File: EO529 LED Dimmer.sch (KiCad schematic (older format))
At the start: 47 parts, among them J1 VBat, Q1 BC639, Q2 BC639, Q3 BC639, Q4 BC639, U1 NE556, U2 NE556

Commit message: Revision to circuit
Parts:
- removed C2: 10n, Capacitor_THT:C_Disc_D5.0mm_W2.5mm_P5.00mm, symbol Device:C_Small
- removed D1, D2, D3, D4, D6, D7, D8, D9: 1N4148, Diode_THT:D_DO-35_SOD27_P7.62mm_Horizontal, symbol Device:D_Small
- removed D10: LED_RGBA, LED_THT:LED_BL-FL7680RGB, symbol Device:LED_RGBA
- removed D5: White, LED_THT:LED_D10.0mm, symbol Device:LED_Small
- removed R6: 1k, Resistor_THT:R_Axial_DIN0207_L6.3mm_D2.5mm_P7.62mm_Horizontal, symbol Device:R_Small
- added C3: 10n, Capacitor_THT:C_Disc_D5.0mm_W2.5mm_P5.00mm, symbol Device:C_Small
- added D1: White, LED_THT:LED_D10.0mm, symbol Device:LED_Small
- added D2: LED_RGBA, LED_THT:LED_BL-FL7680RGB, symbol Device:LED_RGBA
- added R13, R14, R19, R20: 10k, Resistor_THT:R_Axial_DIN0207_L6.3mm_D2.5mm_P7.62mm_Horizontal, symbol Device:R_Small
- added R15, R16, R21, R22, R3: 100k, Resistor_THT:R_Axial_DIN0207_L6.3mm_D2.5mm_P7.62mm_Horizontal, symbol Device:R_Small
- added R17, R23: 1k, Resistor_THT:R_Axial_DIN0207_L6.3mm_D2.5mm_P7.62mm_Horizontal, symbol Device:R_Small
- added R18: 180, Resistor_THT:R_Axial_DIN0207_L6.3mm_D2.5mm_P7.62mm_Horizontal, symbol Device:R_Small
- added R24: 220, Resistor_THT:R_Axial_DIN0207_L6.3mm_D2.5mm_P7.62mm_Horizontal, symbol Device:R_Small
- added U3: LM339, Package_DIP:DIP-14_W7.62mm_Socket, symbol Comparator:LM339
- R1: renamed from R3; value 1k -> 10k
- R10: value 180 -> 100k
- R11: value 220 -> 1k
- R2, R7, R8: value 1k -> 10k
- R4, R9: value 1k -> 100k
- renumbered C3 to C2, R1 to R5, R5 to R6
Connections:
- net Blue: now also D2.3 (BK), R24.2; no longer R12.2
- net GND: now also R10.2, R4.2, C3.2, R16.2, R22.2, U3.12 (V-)
- net Green: now also R12.2, D2.2 (GK); no longer R11.2
- net Red: now also D2.1 (RK)
- net VCC: now also R7.1, D1.2 (A), D2.4 (A), R13.1, R15.1, R19.1, R21.1, R3.1, U3.3 (V+); no longer R4.1, R8.1
- net at R1.2, U1.1 (DIS): now also R2.1
- net at C2.1, U1.2 (THR), U1.6 (TR): now also R2.2, U3.4 (-); no longer RV1.2
- net at U1.5 (Q): no longer R5.2
- net at R8.2: now also C4.1, U1.12 (THR), U1.8 (TR), U3.6 (-); no longer U2.1 (DIS)
- net at U2.2 (THR), U2.6 (TR): now also C6.1, R14.2, U3.8 (-); no longer C7.1, RV3.2
- net at RV1.1: now also R4.1
- net at RV1.3: now also R3.2
- net at RV3.1: now also R16.1
- net at Q3.3 (B): now also R17.1
- net at R11.1: now also Q2.3 (B); no longer Q4.2 (C)
- net at RV3.3: now also R15.2
- net at R12.1: now also Q2.2 (C); no longer Q3.2 (C)
- net at U1.11 (CV): now also C3.1
- net at U1.13 (DIS): now also R7.2, R8.1; no longer R4.2
- net at U1.9 (Q): no longer R2.2
- net at U2.11 (CV): now also C7.1; no longer C6.1
- net at C8.1, U2.12 (THR), U2.8 (TR): now also R20.2, U3.10 (-); no longer RV4.2
- net at R9.2: now also RV2.3; no longer U2.13 (DIS)
- net at U2.9 (Q): no longer R7.2
- net at RV2.1: now also R10.1
- net at RV4.1: now also R22.1
- net at Q4.3 (B): now also R23.1; no longer R7.1
- net at RV4.3: now also R21.2
- new net: RV1.2, U3.5 (+)
- new net: R5.2, U3.2
- new net: R11.2, U3.1
- new net: RV2.2, U3.7 (+)
- new net: R13.2, R14.1, U2.1 (DIS)
- new net: R17.2, U3.14
- new net: RV3.2, U3.9 (+)
- new net: Q3.2 (C), R18.1
- new net: D1.1 (K), R18.2
- new net: R19.2, R20.1, U2.13 (DIS)
- new net: R23.2, U3.13
- new net: RV4.2, U3.11 (+)
- new net: Q4.2 (C), R24.1
- no-connect marks 0 -> 4
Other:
- moved on the sheet: C1, C10, C2, C9, H1, H2, H3, H4, J1, Q1, R1, R5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

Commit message: Fixed broken files
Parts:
- removed U3: LM339, Package_DIP:DIP-14_W7.62mm_Socket, symbol Comparator:LM339
- added U3, U4: LM393, Package_DIP:DIP-8_W7.62mm_Socket, symbol Comparator:LM393
- R24: value 220 -> 150
- R6: value 150 -> 220
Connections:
- net Blue: now also R12.2; no longer R24.2
- net GND: now also U3.4 (V-), U4.4 (V-)
- net Green: now also R6.2; no longer R12.2
- net Red: now also R24.2; no longer R6.2
- net VCC: now also U3.8 (V+), U4.8 (V+)
- net at C2.1, R2.2, U1.2 (THR)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: now also U3.6 (_)
- net at RV1.2: now also U3.5 (+)
- net at R5.2: now also U3.7
- net at C4.1, R8.2, U1.12 (THR)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: now also U4.2 (-)
- net at R11.2: now also U4.1
- net at RV2.2: now also U4.3 (+)
- net at C6.1, R14.2, U2.2 (THR)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: now also U4.6 (_)
- net at R17.2: now also U4.7
- net at RV3.2: now also U4.5 (+)
- net at C8.1, R20.2, U2.12 (THR)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: now also U3.2 (-)
- net at R23.2: now also U3.1
- net at RV4.2: now also U3.3 (+)
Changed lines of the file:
@@
 	1    0    0    -1
 $EndComp
-Text GLabel 4200 1000 1    50   Input ~ 0
+Text GLabel 8300 3000 1    50   Input ~ 0
 Red
 $Comp
@@
 P 4200 1100
 F 0 "R6" H 4141 1054 50  0000 R CNN
-F 1 "150" H 4141 1145 50  0000 R CNN
+F 1 "220" H 4141 1145 50  0000 R CNN
 F 2 "Resistor_THT:R_Axial_DIN0207_L6.3mm_D2.5mm_P7.62mm_Horizontal" H 4200 1100 50  0001 C CNN
 F 3 "~" H 4200 1100 50  0001 C CNN
@@
 	1    0    0    -1
 $EndComp
-Text GLabel 8300 1000 1    50   Input ~ 0
+Text GLabel 4200 1000 1    50   Input ~ 0
 Green
 $Comp
@@
 $EndComp
 $Comp
-L power:GND #PWR020
-U 1 1 6211A0A7
-P 8800 2600
-F 0 "#PWR020" H 8800 2350 50  0001 C CNN
-F 1 "GND" H 8805 2427 50  0000 C CNN
-F 2 "" H 8800 2600 50  0001 C CNN
-F 3 "" H 8800 2600 50  0001 C CNN
-	1    8800 2600
-	1    0    0    -1
-$EndComp
-$Comp
 L power:VCC #PWR019
 U 1 1 62119DEA
-P 8800 2000
-F 0 "#PWR019" H 8800 1850 50  0001 C CNN
-F 1 "VCC" H 8815 2173 50  0000 C CNN
-F 2 "" H 8800 2000 50  0001 C CNN
-F 3 "" H 8800 2000 50  0001 C CNN
-	1    8800 2000
+P 9000 3100
+F 0 "#PWR019" H 9000 2950 50  0001 C CNN
+F 1 "VCC" H 9015 3273 50  0000 C CNN
+F 2 "" H 9000 3100 50  0001 C CNN
+F 3 "" H 9000 3100 50  0001 C CNN
+	1    9000 3100
 	1    0    0    -1
 $EndComp
@@
 	1    0    0    -1
 $EndComp
-Text GLabel 8300 3000 1    50   Input ~ 0
+Text GLabel 8300 1000 1    50   Input ~ 0
 Blue
 $Comp
@@
 P 8300 3100
 F 0 "R24" H 8241 3054 50  0000 R CNN
-F 1 "220" H 8241 3145 50  0000 R CNN
+F 1 "150" H 8241 3145 50  0000 R CNN
 F 2 "Resistor_THT:R_Axial_DIN0207_L6.3mm_D2.5mm_P7.62mm_Horizontal" H 8300 3100 50  0001 C CNN
 F 3 "~" H 8300 3100 50  0001 C CNN
@@
 $EndComp
 $Comp
-L Comparator:LM339 U3
-U 5 1 6229FD5C
-P 8900 2300
-F 0 "U3" H 8858 2346 50  0000 L CNN
-F 1 "LM339" H 8858 2255 50  0000 L CNN
-F 2 "Package_DIP:DIP-14_W7.62mm_Socket" H 8850 2400 50  0001 C CNN
-F 3 "https://www.st.com/resource/en/datasheet/lm139.pdf" H 8950 2500 50  0001 C CNN
-	5    8900 2300
-	1    0    0    -1
-$EndComp
-$Comp
-L Comparator:LM339 U3
-U 2 1 62294DB3
+L Comparator:LM393 U4
+U 1 1 6213A714
 P 7500 1400
-F 0 "U3" H 7500 1767 50  0000 C CNN
-F 1 "LM339" H 7500 1676 50  0000 C CNN
-F 2 "Package_DIP:DIP-14_W7.62mm_Socket" H 7450 1500 50  0001 C CNN
-F 3 "https://www.st.com/resource/en/datasheet/lm139.pdf" H 7550 1600 50  0001 C CNN
-	2    7500 1400
-	1    0    0    -1
-$EndComp
-$Comp
-L Comparator:LM339 U3
-U 1 1 6228FA4A
+F 0 "U4" H 7500 1767 50  0000 C CNN
+F 1 "LM393" H 7500 1676 50  0000 C CNN
+F 2 "Package_DIP:DIP-8_W7.62mm_Socket" H 7500 1400 50  0001 C CNN
+F 3 "http://www.ti.com/lit/ds/symlink/lm393.pdf" H 7500 1400 50  0001 C CNN
+	1    7500 1400
+	1    0    0    -1
+$EndComp
+$Comp
+L Comparator:LM393 U4
+U 2 1 6213FB8E
+P 3400 3400
+F 0 "U4" H 3400 3767 50  0000 C CNN
+F 1 "LM393" H 3400 3676 50  0000 C CNN
+F 2 "Package_DIP:DIP-8_W7.62mm_Socket" H 3400 3400 50  0001 C CNN
+F 3 "http://www.ti.com/lit/ds/symlink/lm393.pdf" H 3400 3400 50  0001 C CNN
+	2    3400 3400
+	1    0    0    -1
+$EndComp
+$Comp
+L power:GND #PWR020
+U 1 1 6211A0A7
+P 9000 3700
+F 0 "#PWR020" H 9000 3450 50  0001 C CNN
+F 1 "GND" H 9005 3527 50  0000 C CNN
+F 2 "" H 9000 3700 50  0001 C CNN
+F 3 "" H 9000 3700 50  0001 C CNN
+	1    9000 3700
+	1    0    0    -1
+$EndComp
+$Comp
+L power:VCC #PWR0101
+U 1 1 62150DA4
+P 9000 1100
+F 0 "#PWR0101" H 9000 950 50  0001 C CNN
+F 1 "VCC" H 9015 1273 50  0000 C CNN
+F 2 "" H 9000 1100 50  0001 C CNN
+F 3 "" H 9000 1100 50  0001 C CNN
+	1    9000 1100
+	1    0    0    -1
+$EndComp
+$Comp
+L power:GND #PWR0102
+U 1 1 62150DB0
+P 9000 1700
+F 0 "#PWR0102" H 9000 1450 50  0001 C CNN
+F 1 "GND" H 9005 1527 50  0000 C CNN
+F 2 "" H 9000 1700 50  0001 C CNN
+F 3 "" H 9000 1700 50  0001 C CNN
+	1    9000 1700
+	1    0    0    -1
+$EndComp
+$Comp
+L Comparator:LM393 U4
+U 3 1 62154E2E
+P 9100 3400
+F 0 "U4" H 9058 3446 50  0000 L CNN
+F 1 "LM393" H 9058 3355 50  0000 L CNN
+F 2 "Package_DIP:DIP-8_W7.62mm_Socket" H 9100 3400 50  0001 C CNN
+F 3 "http://www.ti.com/lit/ds/symlink/lm393.pdf" H 9100 3400 50  0001 C CNN
+	3    9100 3400
+	1    0    0    -1
+$EndComp
+$Comp
+L Comparator:LM393 U3
+U 3 1 62159A90
+P 9100 1400
+F 0 "U3" H 9058 1446 50  0000 L CNN
+F 1 "LM393" H 9058 1355 50  0000 L CNN
+F 2 "Package_DIP:DIP-8_W7.62mm_Socket" H 9100 1400 50  0001 C CNN
+F 3 "http://www.ti.com/lit/ds/symlink/lm393.pdf" H 9100 1400 50  0001 C CNN
+	3    9100 1400
+	1    0    0    -1
+$EndComp
+$Comp
+L Comparator:LM393 U3
+U 2 1 62160E38
 P 3400 1400
 F 0 "U3" H 3400 1767 50  0000 C CNN
-F 1 "LM339" H 3400 1676 50  0000 C CNN
-F 2 "Package_DIP:DIP-14_W7.62mm_Socket" H 3350 1500 50  0001 C CNN
-F 3 "https://www.st.com/resource/en/datasheet/lm139.pdf" H 3450 1600 50  0001 C CNN
-	1    3400 1400
-	1    0    0    -1
-$EndComp
-$Comp
-L Comparator:LM339 U3
-U 3 1 62295A64
+F 1 "LM393" H 3400 1676 50  0000 C CNN
+F 2 "Package_DIP:DIP-8_W7.62mm_Socket" H 3400 1400 50  0001 C CNN
+F 3 "http://www.ti.com/lit/ds/symlink/lm393.pdf" H 3400 1400 50  0001 C CNN
+	2    3400 1400
+	1    0    0    -1
+$EndComp
+$Comp
+L Comparator:LM393 U3
+U 1 1 62160953
 P 7500 3400
 F 0 "U3" H 7500 3767 50  0000 C CNN
-F 1 "LM339" H 7500 3676 50  0000 C CNN
-F 2 "Package_DIP:DIP-14_W7.62mm_Socket" H 7450 3500 50  0001 C CNN
-F 3 "https://www.st.com/resource/en/datasheet/lm139.pdf" H 7550 3600 50  0001 C CNN
-	3    7500 3400
-	1    0    0    -1
-$EndComp
-$Comp
-L Comparator:LM339 U3
-U 4 1 62296761
-P 3400 3400
-F 0 "U3" H 3400 3767 50  0000 C CNN
-F 1 "LM339" H 3400 3676 50  0000 C CNN
-F 2 "Package_DIP:DIP-14_W7.62mm_Socket" H 3350 3500 50  0001 C CNN
-F 3 "https://www.st.com/resource/en/datasheet/lm139.pdf" H 3450 3600 50  0001 C CNN
-	4    3400 3400
-	1    0    0    -1
-$EndComp
+F 1 "LM393" H 7500 3676 50  0000 C CNN
+F 2 "Package_DIP:DIP-8_W7.62mm_Socket" H 7500 3400 50  0001 C CNN
+F 3 "http://www.ti.com/lit/ds/symlink/lm393.pdf" H 7500 3400 50  0001 C CNN
+	1    7500 3400
+	1    0    0    -1
+$EndComp

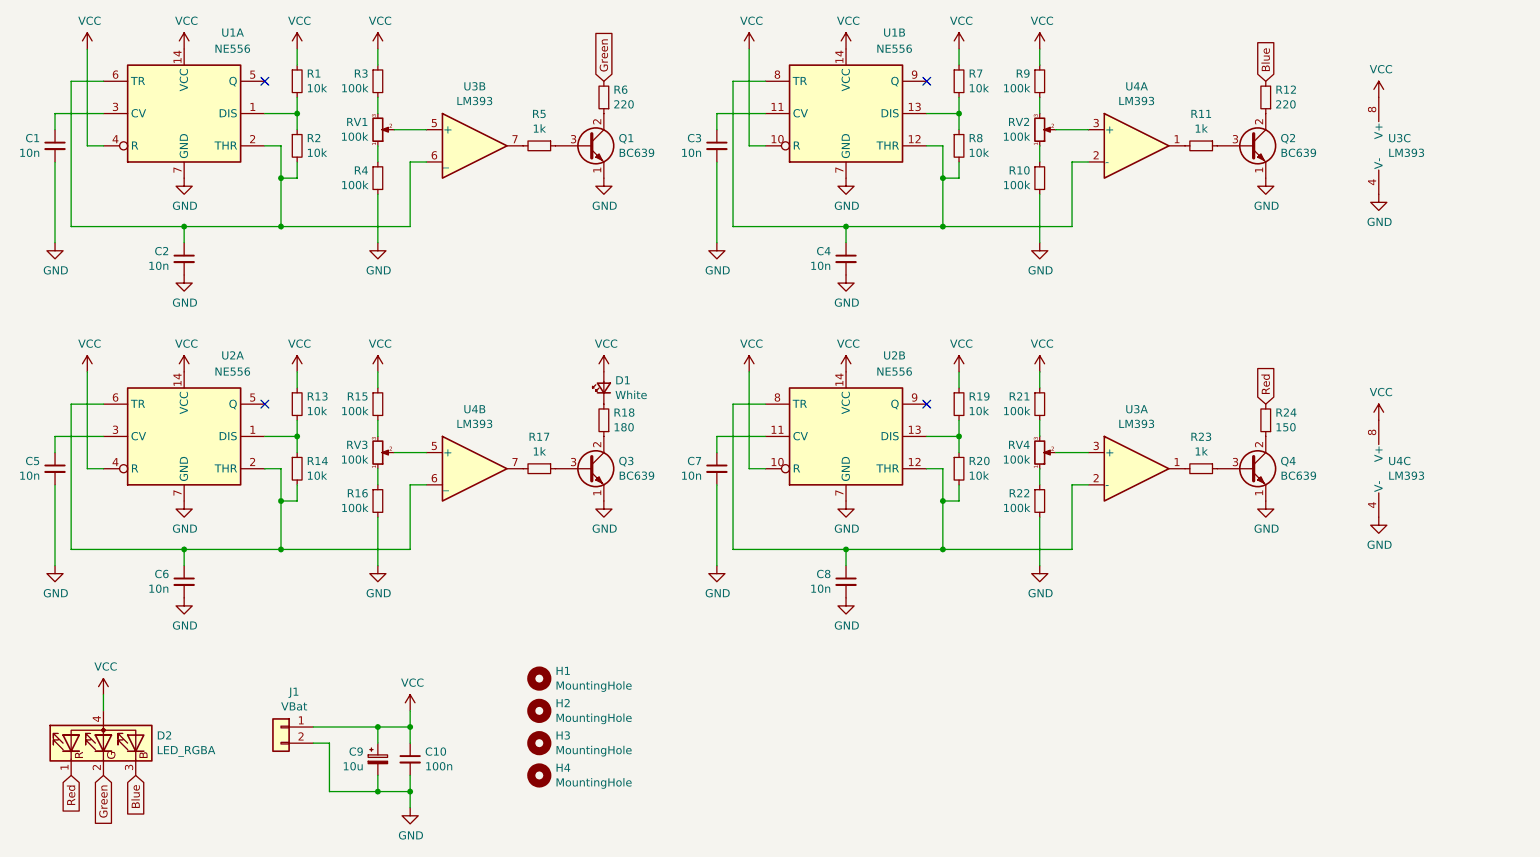
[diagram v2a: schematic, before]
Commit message: Revert "Fixed broken files"
This reverts commit e50aa6ede737ee02b3ead64743985b0a59545fc6.
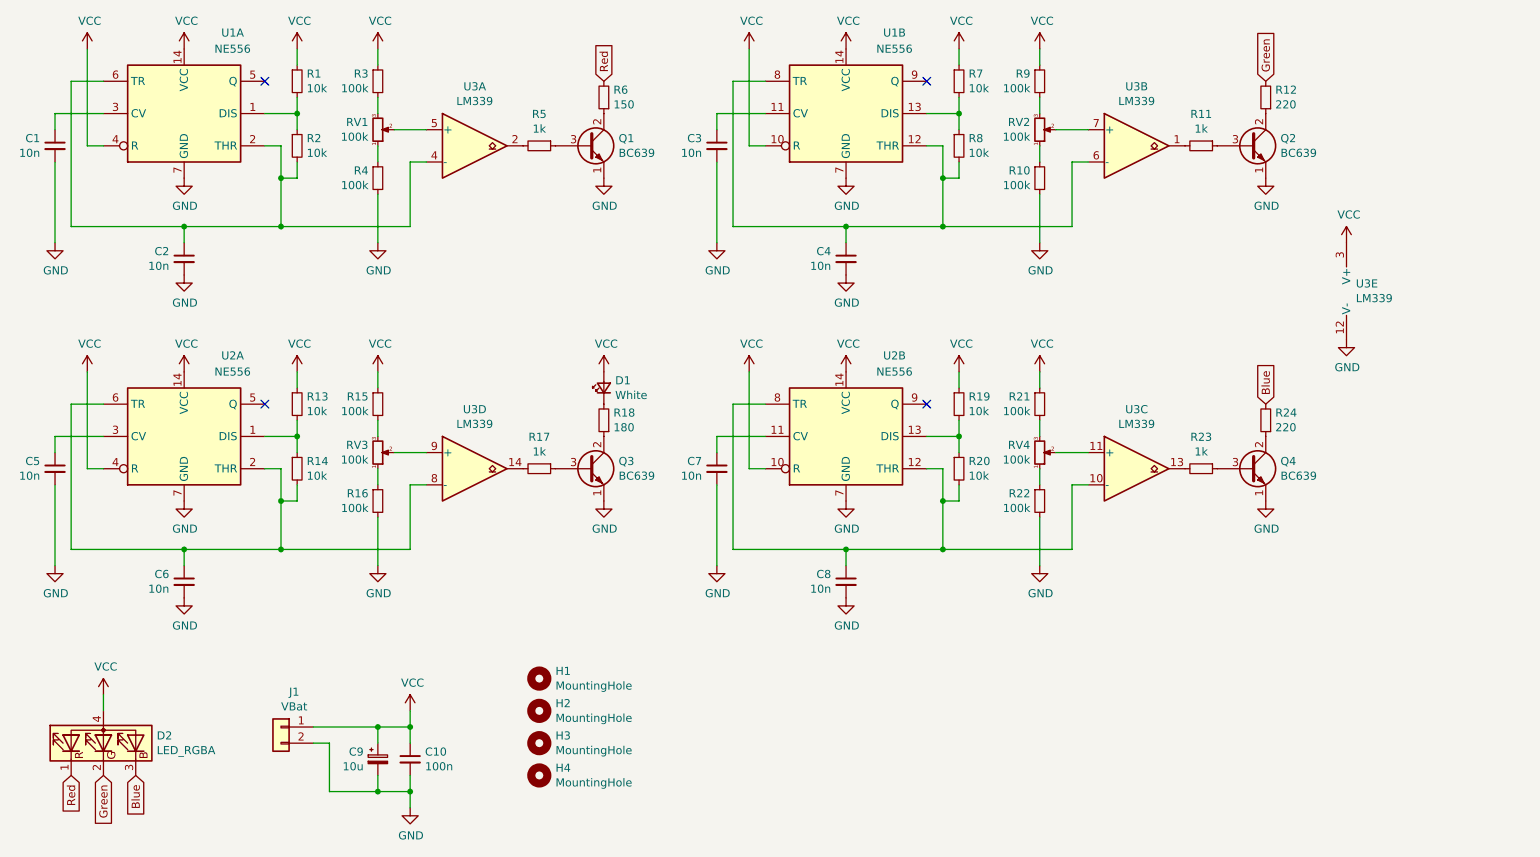
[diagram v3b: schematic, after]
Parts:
- removed U3, U4: LM393, Package_DIP:DIP-8_W7.62mm_Socket, symbol Comparator:LM393
- added U3: LM339, Package_DIP:DIP-14_W7.62mm_Socket, symbol Comparator:LM339
- R24: value 150 -> 220
- R6: value 220 -> 150
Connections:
- net Blue: now also R24.2; no longer R12.2
- net GND: now also U3.12 (V-)
- net Green: now also R12.2; no longer R6.2
- net Red: now also R6.2; no longer R24.2
- net VCC: now also U3.3 (V+)
- net at C2.1, R2.2, U1.2 (THR)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: now also U3.4 (-)
- net at RV1.2: now also U3.5 (+)
- net at R5.2: now also U3.2
- net at C4.1, R8.2, U1.12 (THR)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: now also U3.6 (-)
- net at R11.2: now also U3.1
- net at RV2.2: now also U3.7 (+)
- net at RV3.2: now also U3.9 (+)
- net at C6.1, R14.2, U2.2 (THR)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: now also U3.8 (-)
- net at R17.2: now also U3.14
- net at C8.1, R20.2, U2.12 (THR)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: now also U3.10 (-)
- net at R23.2: now also U3.13
- net at RV4.2: now also U3.11 (+)
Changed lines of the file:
@@
 	1    0    0    -1
 $EndComp
-Text GLabel 8300 3000 1    50   Input ~ 0
+Text GLabel 4200 1000 1    50   Input ~ 0
 Red
 $Comp
@@
 P 4200 1100
 F 0 "R6" H 4141 1054 50  0000 R CNN
-F 1 "220" H 4141 1145 50  0000 R CNN
+F 1 "150" H 4141 1145 50  0000 R CNN
 F 2 "Resistor_THT:R_Axial_DIN0207_L6.3mm_D2.5mm_P7.62mm_Horizontal" H 4200 1100 50  0001 C CNN
 F 3 "~" H 4200 1100 50  0001 C CNN
@@
 	1    0    0    -1
 $EndComp
-Text GLabel 4200 1000 1    50   Input ~ 0
+Text GLabel 8300 1000 1    50   Input ~ 0
 Green
 $Comp
@@
 $EndComp
 $Comp
+L power:GND #PWR020
+U 1 1 6211A0A7
+P 8800 2600
+F 0 "#PWR020" H 8800 2350 50  0001 C CNN
+F 1 "GND" H 8805 2427 50  0000 C CNN
+F 2 "" H 8800 2600 50  0001 C CNN
+F 3 "" H 8800 2600 50  0001 C CNN
+	1    8800 2600
+	1    0    0    -1
+$EndComp
+$Comp
 L power:VCC #PWR019
 U 1 1 62119DEA
-P 9000 3100
-F 0 "#PWR019" H 9000 2950 50  0001 C CNN
-F 1 "VCC" H 9015 3273 50  0000 C CNN
-F 2 "" H 9000 3100 50  0001 C CNN
-F 3 "" H 9000 3100 50  0001 C CNN
-	1    9000 3100
+P 8800 2000
+F 0 "#PWR019" H 8800 1850 50  0001 C CNN
+F 1 "VCC" H 8815 2173 50  0000 C CNN
+F 2 "" H 8800 2000 50  0001 C CNN
+F 3 "" H 8800 2000 50  0001 C CNN
+	1    8800 2000
 	1    0    0    -1
 $EndComp
@@
 	1    0    0    -1
 $EndComp
-Text GLabel 8300 1000 1    50   Input ~ 0
+Text GLabel 8300 3000 1    50   Input ~ 0
 Blue
 $Comp
@@
 P 8300 3100
 F 0 "R24" H 8241 3054 50  0000 R CNN
-F 1 "150" H 8241 3145 50  0000 R CNN
+F 1 "220" H 8241 3145 50  0000 R CNN
 F 2 "Resistor_THT:R_Axial_DIN0207_L6.3mm_D2.5mm_P7.62mm_Horizontal" H 8300 3100 50  0001 C CNN
 F 3 "~" H 8300 3100 50  0001 C CNN
@@
 $EndComp
 $Comp
-L Comparator:LM393 U4
-U 1 1 6213A714
+L Comparator:LM339 U3
+U 5 1 6229FD5C
+P 8900 2300
+F 0 "U3" H 8858 2346 50  0000 L CNN
+F 1 "LM339" H 8858 2255 50  0000 L CNN
+F 2 "Package_DIP:DIP-14_W7.62mm_Socket" H 8850 2400 50  0001 C CNN
+F 3 "https://www.st.com/resource/en/datasheet/lm139.pdf" H 8950 2500 50  0001 C CNN
+	5    8900 2300
+	1    0    0    -1
+$EndComp
+$Comp
+L Comparator:LM339 U3
+U 2 1 62294DB3
 P 7500 1400
-F 0 "U4" H 7500 1767 50  0000 C CNN
-F 1 "LM393" H 7500 1676 50  0000 C CNN
-F 2 "Package_DIP:DIP-8_W7.62mm_Socket" H 7500 1400 50  0001 C CNN
-F 3 "http://www.ti.com/lit/ds/symlink/lm393.pdf" H 7500 1400 50  0001 C CNN
-	1    7500 1400
-	1    0    0    -1
-$EndComp
-$Comp
-L Comparator:LM393 U4
-U 2 1 6213FB8E
-P 3400 3400
-F 0 "U4" H 3400 3767 50  0000 C CNN
-F 1 "LM393" H 3400 3676 50  0000 C CNN
-F 2 "Package_DIP:DIP-8_W7.62mm_Socket" H 3400 3400 50  0001 C CNN
-F 3 "http://www.ti.com/lit/ds/symlink/lm393.pdf" H 3400 3400 50  0001 C CNN
-	2    3400 3400
-	1    0    0    -1
-$EndComp
-$Comp
-L power:GND #PWR020
-U 1 1 6211A0A7
-P 9000 3700
-F 0 "#PWR020" H 9000 3450 50  0001 C CNN
-F 1 "GND" H 9005 3527 50  0000 C CNN
-F 2 "" H 9000 3700 50  0001 C CNN
-F 3 "" H 9000 3700 50  0001 C CNN
-	1    9000 3700
-	1    0    0    -1
-$EndComp
-$Comp
-L power:VCC #PWR0101
-U 1 1 62150DA4
-P 9000 1100
-F 0 "#PWR0101" H 9000 950 50  0001 C CNN
-F 1 "VCC" H 9015 1273 50  0000 C CNN
-F 2 "" H 9000 1100 50  0001 C CNN
-F 3 "" H 9000 1100 50  0001 C CNN
-	1    9000 1100
-	1    0    0    -1
-$EndComp
-$Comp
-L power:GND #PWR0102
-U 1 1 62150DB0
-P 9000 1700
-F 0 "#PWR0102" H 9000 1450 50  0001 C CNN
-F 1 "GND" H 9005 1527 50  0000 C CNN
-F 2 "" H 9000 1700 50  0001 C CNN
-F 3 "" H 9000 1700 50  0001 C CNN
-	1    9000 1700
-	1    0    0    -1
-$EndComp
-$Comp
-L Comparator:LM393 U4
-U 3 1 62154E2E
-P 9100 3400
-F 0 "U4" H 9058 3446 50  0000 L CNN
-F 1 "LM393" H 9058 3355 50  0000 L CNN
-F 2 "Package_DIP:DIP-8_W7.62mm_Socket" H 9100 3400 50  0001 C CNN
-F 3 "http://www.ti.com/lit/ds/symlink/lm393.pdf" H 9100 3400 50  0001 C CNN
-	3    9100 3400
-	1    0    0    -1
-$EndComp
-$Comp
-L Comparator:LM393 U3
-U 3 1 62159A90
-P 9100 1400
-F 0 "U3" H 9058 1446 50  0000 L CNN
-F 1 "LM393" H 9058 1355 50  0000 L CNN
-F 2 "Package_DIP:DIP-8_W7.62mm_Socket" H 9100 1400 50  0001 C CNN
-F 3 "http://www.ti.com/lit/ds/symlink/lm393.pdf" H 9100 1400 50  0001 C CNN
-	3    9100 1400
-	1    0    0    -1
-$EndComp
-$Comp
-L Comparator:LM393 U3
-U 2 1 62160E38
+F 0 "U3" H 7500 1767 50  0000 C CNN
+F 1 "LM339" H 7500 1676 50  0000 C CNN
+F 2 "Package_DIP:DIP-14_W7.62mm_Socket" H 7450 1500 50  0001 C CNN
+F 3 "https://www.st.com/resource/en/datasheet/lm139.pdf" H 7550 1600 50  0001 C CNN
+	2    7500 1400
+	1    0    0    -1
+$EndComp
+$Comp
+L Comparator:LM339 U3
+U 1 1 6228FA4A
 P 3400 1400
 F 0 "U3" H 3400 1767 50  0000 C CNN
-F 1 "LM393" H 3400 1676 50  0000 C CNN
-F 2 "Package_DIP:DIP-8_W7.62mm_Socket" H 3400 1400 50  0001 C CNN
-F 3 "http://www.ti.com/lit/ds/symlink/lm393.pdf" H 3400 1400 50  0001 C CNN
-	2    3400 1400
-	1    0    0    -1
-$EndComp
-$Comp
-L Comparator:LM393 U3
-U 1 1 62160953
+F 1 "LM339" H 3400 1676 50  0000 C CNN
+F 2 "Package_DIP:DIP-14_W7.62mm_Socket" H 3350 1500 50  0001 C CNN
+F 3 "https://www.st.com/resource/en/datasheet/lm139.pdf" H 3450 1600 50  0001 C CNN
+	1    3400 1400
+	1    0    0    -1
+$EndComp
+$Comp
+L Comparator:LM339 U3
+U 3 1 62295A64
 P 7500 3400
 F 0 "U3" H 7500 3767 50  0000 C CNN
-F 1 "LM393" H 7500 3676 50  0000 C CNN
-F 2 "Package_DIP:DIP-8_W7.62mm_Socket" H 7500 3400 50  0001 C CNN
-F 3 "http://www.ti.com/lit/ds/symlink/lm393.pdf" H 7500 3400 50  0001 C CNN
-	1    7500 3400
-	1    0    0    -1
-$EndComp
+F 1 "LM339" H 7500 3676 50  0000 C CNN
+F 2 "Package_DIP:DIP-14_W7.62mm_Socket" H 7450 3500 50  0001 C CNN
+F 3 "https://www.st.com/resource/en/datasheet/lm139.pdf" H 7550 3600 50  0001 C CNN
+	3    7500 3400
+	1    0    0    -1
+$EndComp
+$Comp
+L Comparator:LM339 U3
+U 4 1 62296761
+P 3400 3400
+F 0 "U3" H 3400 3767 50  0000 C CNN
+F 1 "LM339" H 3400 3676 50  0000 C CNN
+F 2 "Package_DIP:DIP-14_W7.62mm_Socket" H 3350 3500 50  0001 C CNN
+F 3 "https://www.st.com/resource/en/datasheet/lm139.pdf" H 3450 3600 50  0001 C CNN
+	4    3400 3400
+	1    0    0    -1
+$EndComp
